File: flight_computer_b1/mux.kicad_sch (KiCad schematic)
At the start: 1 part, among them U10 CD74HC4067SM

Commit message: flight computer: added pyro circuit and digikey part numbers
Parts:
- U10: DIGIKEY PART N (none) -> 296-9226-1-ND
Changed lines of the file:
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@@
+			)
+		)
+		(property "DIGIKEY PART N" "296-9226-1-ND"
+			(at 135.89 87.63 0)
+			(effects
+				(font
+					(size 1.27 1.27)
+				)
+				(hide yes)
 			)
 		)

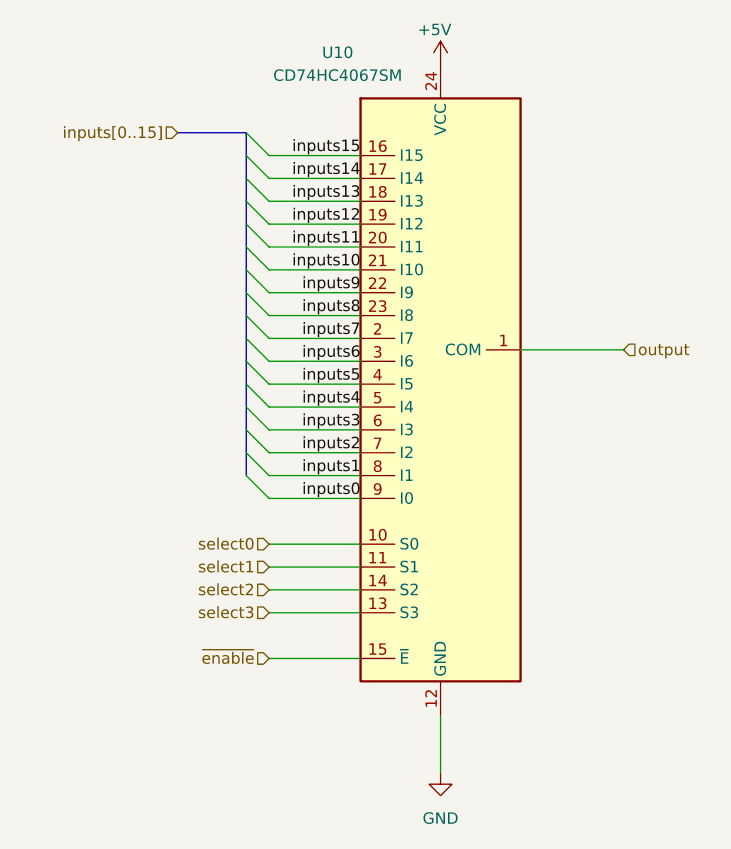
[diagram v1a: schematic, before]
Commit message: flight computer: routing updates
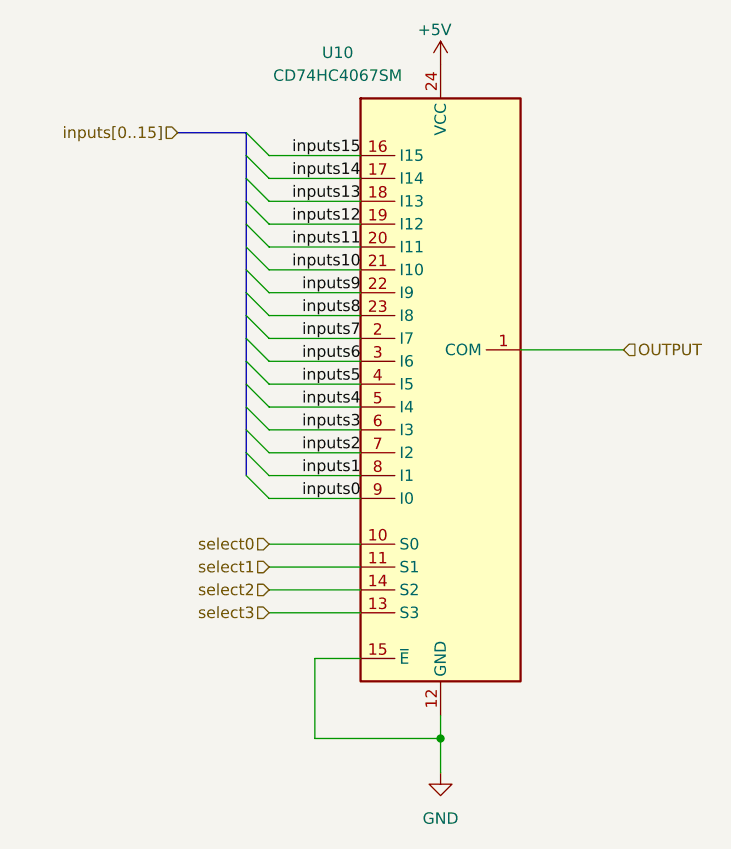
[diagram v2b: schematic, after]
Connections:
- net ~{enable} is gone; now on net GND: U10.15 (~{E})
- net output renamed OUTPUT
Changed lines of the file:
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@@
 		(company "Purdue Space Program Liquids")
 	)
+	(junction
+		(at 135.89 125.73)
+		(diameter 0)
+		(color 0 0 0 0)
+	)
 	(bus_entry
 		(at 114.3 73.66)
@@
 	(wire
 		(pts
+			(xy 121.92 116.84) (xy 127 116.84)
+		)
+		(stroke
+			(width 0)
+			(type default)
+		)
+	)
+	(wire
+		(pts
 			(xy 116.84 106.68) (xy 127 106.68)
 		)
@@
 	(wire
 		(pts
+			(xy 135.89 125.73) (xy 135.89 129.54)
+		)
+		(stroke
+			(width 0)
+			(type default)
+		)
+	)
+	(wire
+		(pts
 			(xy 116.84 86.36) (xy 127 86.36)
 		)
@@
 	(wire
 		(pts
-			(xy 116.84 116.84) (xy 127 116.84)
-		)
-		(stroke
-			(width 0)
-			(type default)
-		)
-	)
-	(wire
-		(pts
 			(xy 116.84 96.52) (xy 127 96.52)
 		)
@@
 	(wire
 		(pts
+			(xy 121.92 125.73) (xy 135.89 125.73)
+		)
+		(stroke
+			(width 0)
+			(type default)
+		)
+	)
+	(wire
+		(pts
 			(xy 116.84 88.9) (xy 127 88.9)
 		)
@@
 	(wire
 		(pts
-			(xy 135.89 123.19) (xy 135.89 129.54)
+			(xy 135.89 123.19) (xy 135.89 125.73)
 		)
 		(stroke
@@
 		(pts
 			(xy 116.84 71.12) (xy 127 71.12)
+		)
+		(stroke
+			(width 0)
+			(type default)
+		)
+	)
+	(wire
+		(pts
+			(xy 121.92 116.84) (xy 121.92 125.73)
 		)
 		(stroke
@@
 		)
 	)
-	(hierarchical_label "~{enable}"
-		(shape input)
-		(at 116.84 116.84 180)
-		(effects
-			(font
-				(size 1.27 1.27)
-			)
-			(justify right)
-		)
-	)
 	(hierarchical_label "select2"
 		(shape input)
@@
 		)
 	)
-	(hierarchical_label "output"
+	(hierarchical_label "OUTPUT"
 		(shape input)
 		(at 156.21 82.55 0)
@@
 		(on_board yes)
 		(dnp no)
-		(property "Reference" "#PWR064"
+		(property "Reference" "#PWR065"
 			(at 135.89 54.61 0)
 			(effects
@@
 			(project "flight_computer"
 				(path "/b71a7b79-cdb5-4e38-a72c-0daaa3474f05/73ecdfe5-1123-4217-8df2-7ecc56cfe43e"
-					(reference "#PWR064")
+					(reference "#PWR065")
 					(unit 1)
 				)
@@
 		(dnp no)
 		(fields_autoplaced yes)
-		(property "Reference" "#PWR063"
+		(property "Reference" "#PWR066"
 			(at 135.89 135.89 0)
 			(effects
@@
 			(project "flight_computer"
 				(path "/b71a7b79-cdb5-4e38-a72c-0daaa3474f05/73ecdfe5-1123-4217-8df2-7ecc56cfe43e"
-					(reference "#PWR063")
+					(reference "#PWR066")
 					(unit 1)
 				)

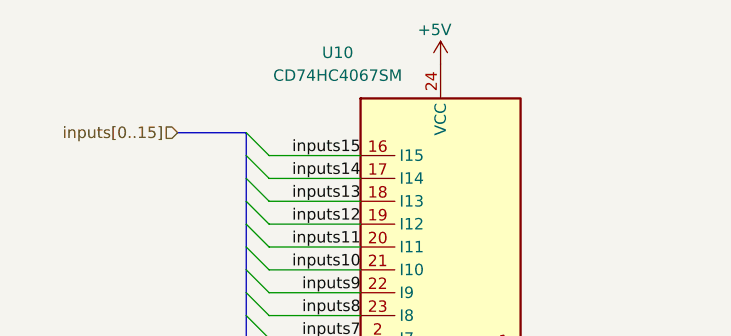
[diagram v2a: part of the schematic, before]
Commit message: flight computer: new pyro circuit
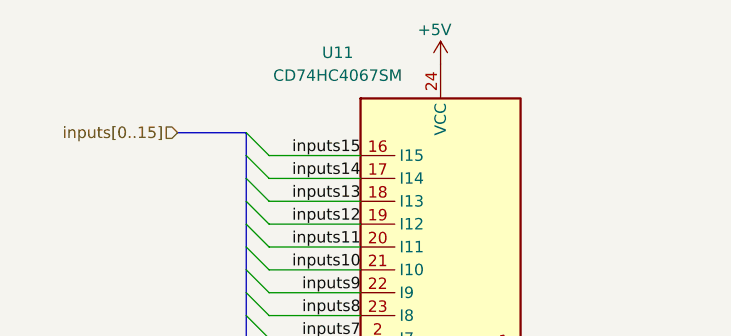
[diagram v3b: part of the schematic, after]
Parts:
- renumbered U10 to U11
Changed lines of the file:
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@@
 		(on_board yes)
 		(dnp no)
-		(property "Reference" "U10"
+		(property "Reference" "U11"
 			(at 124.46 49.53 0)
 			(effects
@@
 			(project "flight_computer"
 				(path "/b71a7b79-cdb5-4e38-a72c-0daaa3474f05/73ecdfe5-1123-4217-8df2-7ecc56cfe43e"
-					(reference "U10")
+					(reference "U11")
 					(unit 1)
 				)
